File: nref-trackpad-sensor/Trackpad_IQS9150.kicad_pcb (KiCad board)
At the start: 2 copper layers, 105.5 x 53.3 mm, 44 parts, among them CN1 FPC_6PIN, IC1 IQS9150-000QFR

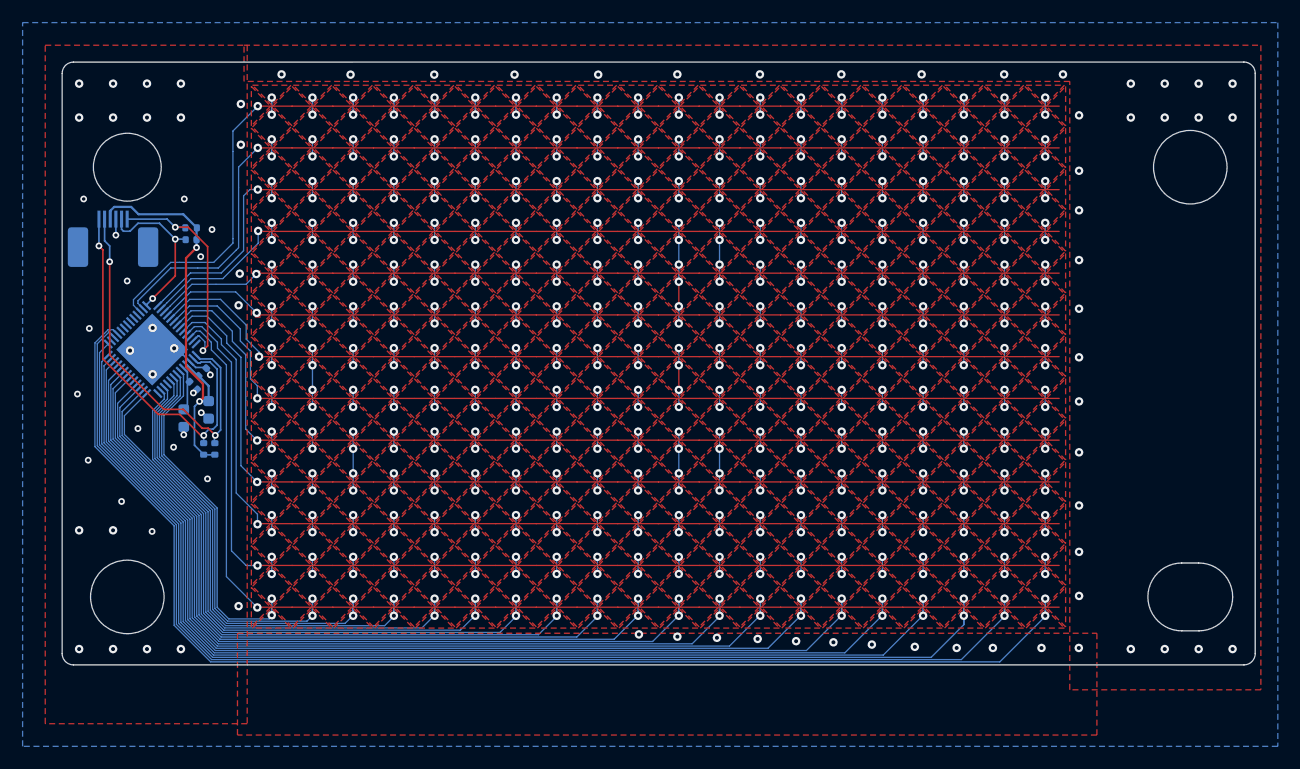
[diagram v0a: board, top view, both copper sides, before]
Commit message: trackpad: pcb traces adjustment for prod
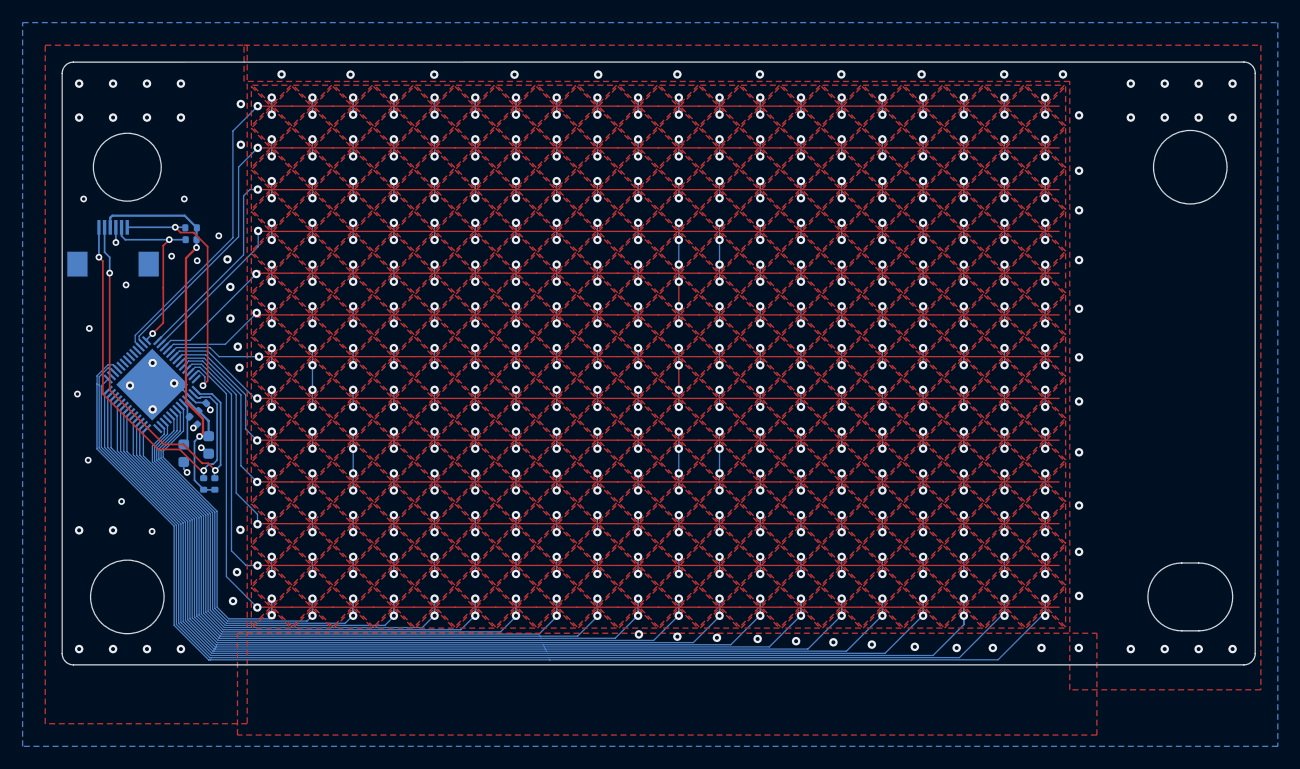
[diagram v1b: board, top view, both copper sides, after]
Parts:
- CN1: footprint Trackpad_IQS9150:FPC6PIN -> Connector_FFC-FPC:Hirose_FH12-6S-0.5SH_1x06-1MP_P0.50mm_Horizontal
- moved C1 3.10 mm to (115.5, 112.0)
- moved R2 3.10 mm to (116.0, 115.4)
- moved R3 3.10 mm to (115.0, 115.4)
- moved C2 3.10 mm to (114.9, 108.6)
- moved C3 3.10 mm to (113.3, 112.7)
- moved C4 3.10 mm to (114.1, 109.8)
- moved IC1 3.10 mm to (110.5, 106.6)
- moved CN1 1.56 mm to (107.0, 94.6)
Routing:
- net /Trackpad_IQS9150_1/ROW6: track 85.0 -> 80.2 mm
- net /Trackpad_IQS9150_1/ROW5: track 87.8 -> 83.2 mm
- net /Trackpad_IQS9150_1/COL7: track 71.8 -> 67.3 mm
- net /Trackpad_IQS9150_1/COL8: track 76.1 -> 71.7 mm
- net /Trackpad_IQS9150_1/COL9: track 80.4 -> 76.0 mm
- net /Trackpad_IQS9150_1/COL10: track 84.5 -> 80.2 mm
- net /Trackpad_IQS9150_1/ROW4: track 90.3 -> 86.1 mm
- net /Trackpad_IQS9150_1/COL11: track 97.8 -> 93.7 mm
- net /Trackpad_IQS9150_1/COL12: track 97.7 -> 93.7 mm
- net /Trackpad_IQS9150_1/COL13: track 97.5 -> 93.6 mm
- net /Trackpad_IQS9150_1/COL14: track 101.8 -> 97.9 mm
- net /Trackpad_IQS9150_1/ROW3: track 92.9 -> 89.3 mm
- net /Trackpad_IQS9150_1/VDD: track 36.8 -> 40.4 mm
- net /Trackpad_IQS9150_1/COL15: track 106.3 -> 102.7 mm
- net /Trackpad_IQS9150_1/COL16: track 110.5 -> 107.0 mm
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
